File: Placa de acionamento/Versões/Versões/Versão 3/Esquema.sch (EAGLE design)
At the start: 23 parts, among them Q1 IRF540, Q2 IRF540, Q3 IRF540

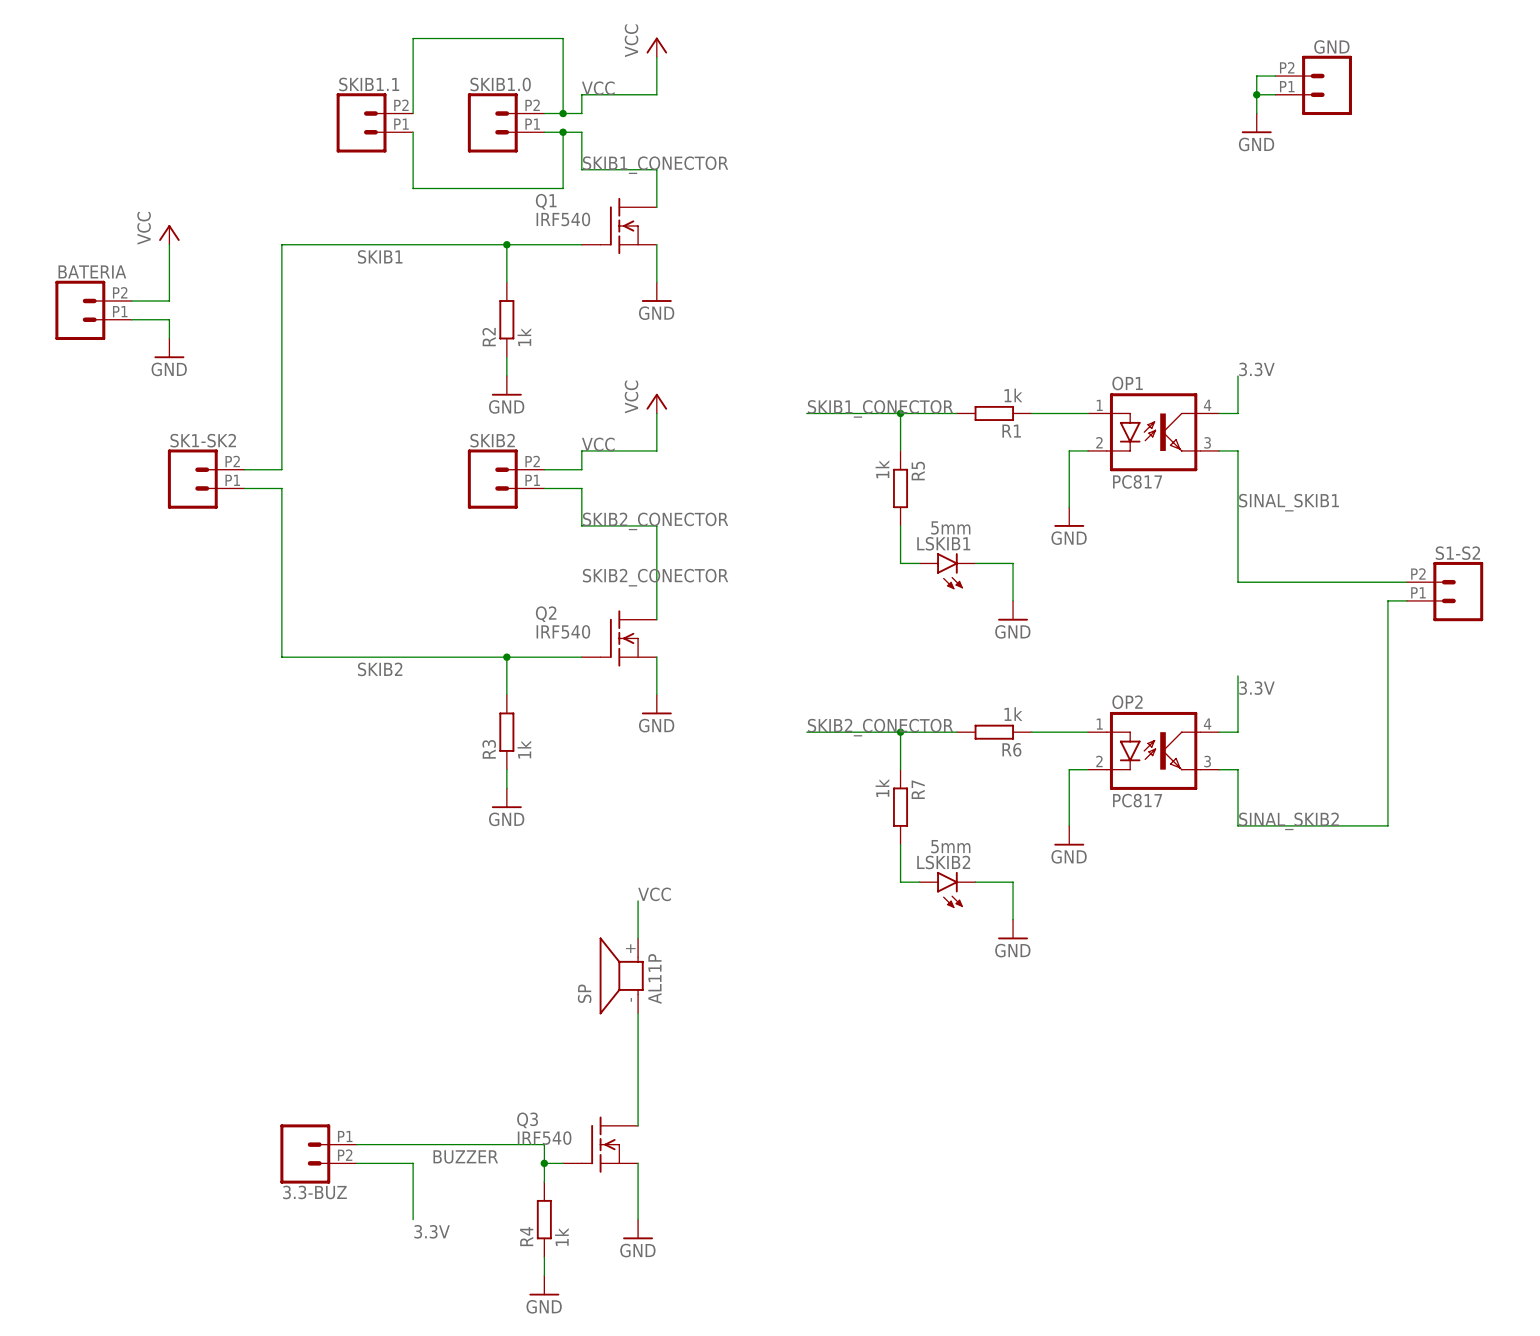
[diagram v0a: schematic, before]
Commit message: CHORE: trocando conectores JST
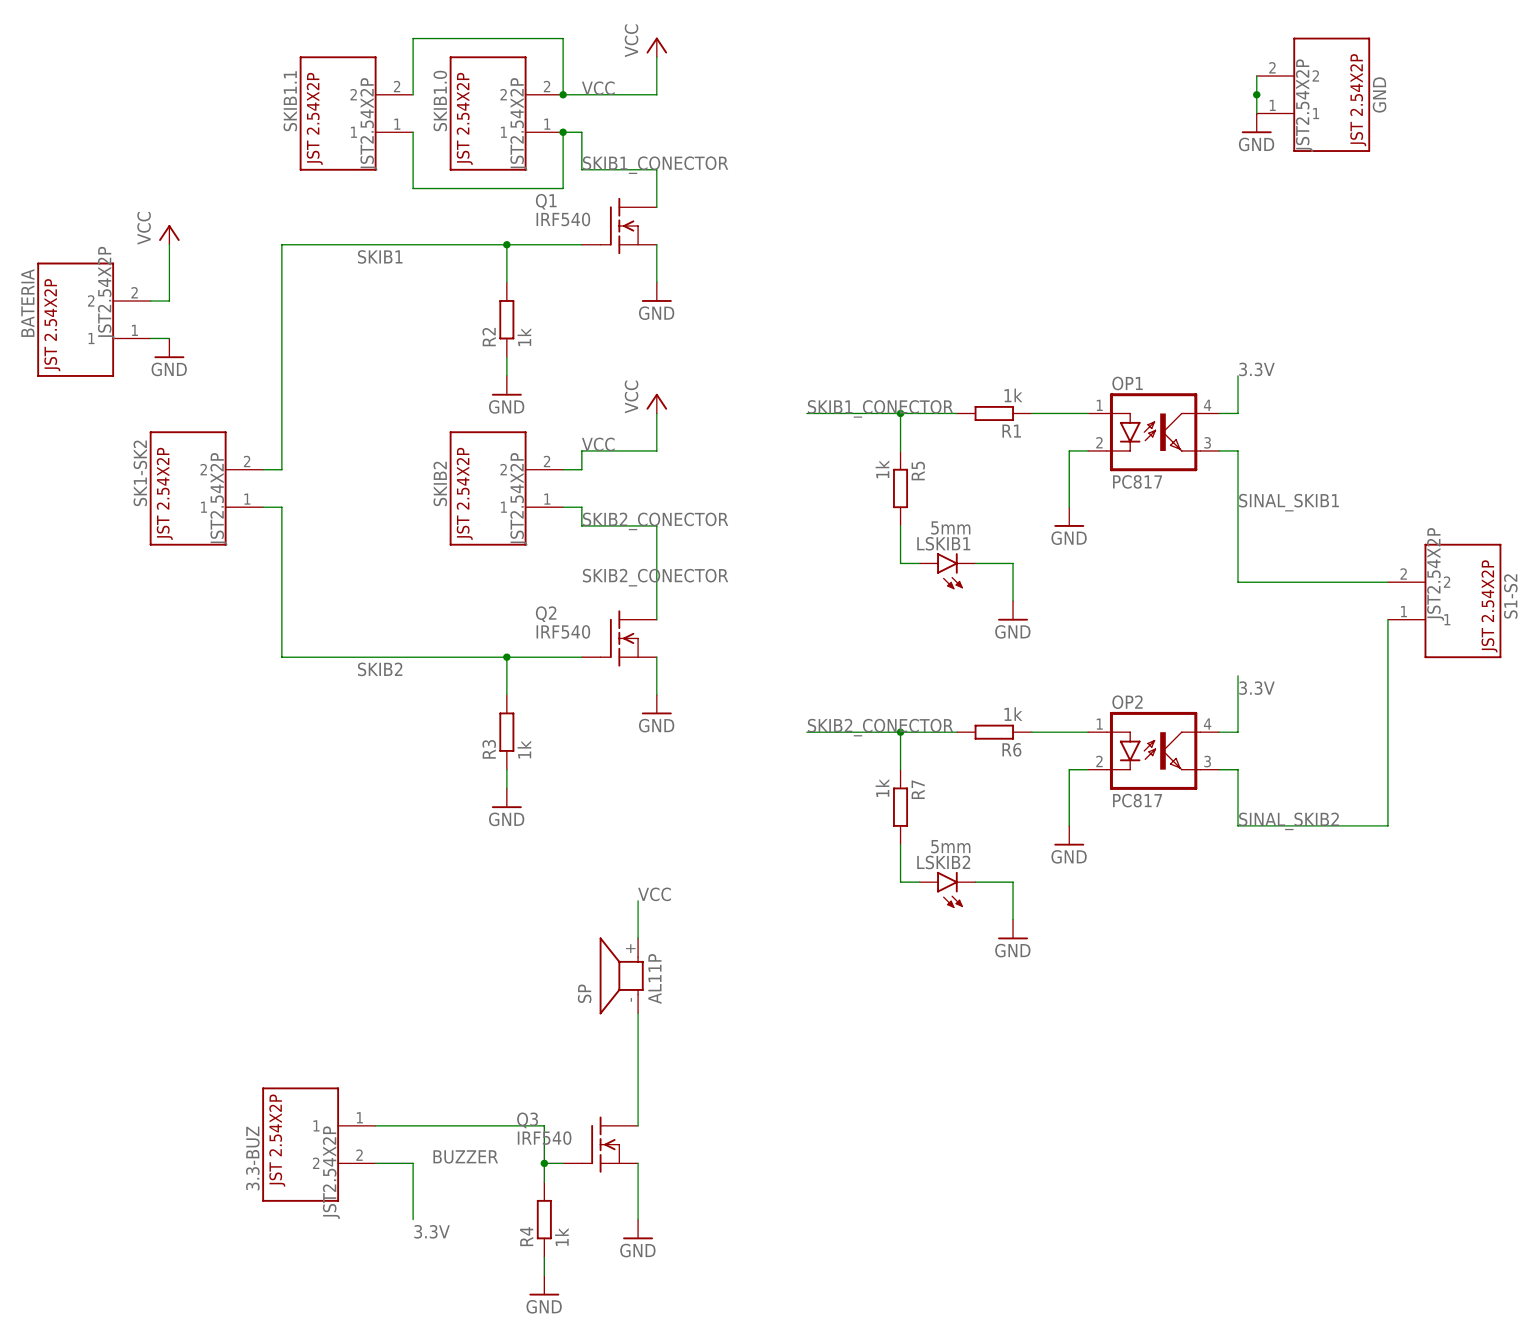
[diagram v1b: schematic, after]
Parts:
- 3.3-BUZ, BATERIA, GND, S1-S2, SK1-SK2, SKIB1.0, SKIB1.1, SKIB2: value (none) -> JST2.54X2P; device SparkFun-Connectors:CONN_022.54MM_SCREWTERM -> CRD:JST2.54X2P

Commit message: CHORE: adicionando pads ovais
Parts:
- LSKIB1, LSKIB2: device led:LED5MM -> led-modificada:LED5MM
- R1, R2, R3, R4, R5, R6, R7: device rcl:R-EU_0207/10 -> rcl-modificada:R-EU_0207/10
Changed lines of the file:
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@@
 <part name="Q3" library="transistor-fet" library_urn="urn:adsk.eagle:library:396" deviceset="IRF540" device="" package3d_urn="urn:adsk.eagle:package:28520/1" override_package3d_urn="urn:adsk.eagle:package:49474191/2" override_package_urn="urn:adsk.eagle:footprint:28453/1"/>
 <part name="GND2" library="supply1" library_urn="urn:adsk.eagle:library:371" deviceset="GND" device=""/>
-<part name="SP" library="buzzer" library_urn="urn:adsk.eagle:library:113" deviceset="AL11P" device="" package3d_urn="urn:adsk.eagle:package:5308/1" override_package3d_urn="urn:adsk.eagle:package:49474189/2" override_package_urn="urn:adsk.eagle:footprint:5250/1"/>
-<part name="R2" library="rcl" library_urn="urn:adsk.eagle:library:334" deviceset="R-EU_" device="0207/10" package3d_urn="urn:adsk.eagle:package:23491/2" value="1k"/>
-<part name="R3" library="rcl" library_urn="urn:adsk.eagle:library:334" deviceset="R-EU_" device="0207/10" package3d_urn="urn:adsk.eagle:package:23491/2" value="1k"/>
-<part name="R4" library="rcl" library_urn="urn:adsk.eagle:library:334" deviceset="R-EU_" device="0207/10" package3d_urn="urn:adsk.eagle:package:23491/2" value="1k"/>
+<part name="SP" library="buzzer" deviceset="AL11P" device="" package3d_urn="urn:adsk.eagle:package:5308/1" override_package3d_urn="urn:adsk.eagle:package:49474189/2" override_package_urn="urn:adsk.eagle:footprint:5250/1" override_locally_modified="yes"/>
+<part name="R2" library="rcl-modificada" deviceset="R-EU_" device="0207/10" package3d_urn="urn:adsk.eagle:package:23491/2" value="1k"/>
+<part name="R3" library="rcl-modificada" deviceset="R-EU_" device="0207/10" package3d_urn="urn:adsk.eagle:package:23491/2" value="1k"/>
+<part name="R4" library="rcl-modificada" deviceset="R-EU_" device="0207/10" package3d_urn="urn:adsk.eagle:package:23491/2" value="1k"/>
 <part name="GND1" library="supply1" library_urn="urn:adsk.eagle:library:371" deviceset="GND" device=""/>
 <part name="GND3" library="supply1" library_urn="urn:adsk.eagle:library:371" deviceset="GND" device=""/>
 <part name="GND4" library="supply1" library_urn="urn:adsk.eagle:library:371" deviceset="GND" device=""/>
 <part name="OP1" library="optocoupler" library_urn="urn:adsk.eagle:library:320" deviceset="PC817" device="" package3d_urn="urn:adsk.eagle:package:21938/1" override_package3d_urn="urn:adsk.eagle:package:49474184/2" override_package_urn="urn:adsk.eagle:footprint:21858/1"/>
-<part name="R1" library="rcl" library_urn="urn:adsk.eagle:library:334" deviceset="R-EU_" device="0207/10" package3d_urn="urn:adsk.eagle:package:23491/2" value="1k"/>
-<part name="R5" library="rcl" library_urn="urn:adsk.eagle:library:334" deviceset="R-EU_" device="0207/10" package3d_urn="urn:adsk.eagle:package:23491/2" value="1k"/>
-<part name="LSKIB1" library="led" library_urn="urn:adsk.eagle:library:259" deviceset="LED" device="5MM" package3d_urn="urn:adsk.eagle:package:15799/2" value="5mm"/>
+<part name="R1" library="rcl-modificada" deviceset="R-EU_" device="0207/10" package3d_urn="urn:adsk.eagle:package:23491/2" value="1k"/>
+<part name="R5" library="rcl-modificada" deviceset="R-EU_" device="0207/10" package3d_urn="urn:adsk.eagle:package:23491/2" value="1k"/>
+<part name="LSKIB1" library="led-modificada" deviceset="LED" device="5MM" package3d_urn="urn:adsk.eagle:package:15799/2" value="5mm"/>
 <part name="GND5" library="supply1" library_urn="urn:adsk.eagle:library:371" deviceset="GND" device=""/>
 <part name="GND7" library="supply1" library_urn="urn:adsk.eagle:library:371" deviceset="GND" device=""/>
 <part name="OP2" library="optocoupler" library_urn="urn:adsk.eagle:library:320" deviceset="PC817" device="" package3d_urn="urn:adsk.eagle:package:21938/1" override_package3d_urn="urn:adsk.eagle:package:49474187/2" override_package_urn="urn:adsk.eagle:footprint:21858/1"/>
-<part name="R6" library="rcl" library_urn="urn:adsk.eagle:library:334" deviceset="R-EU_" device="0207/10" package3d_urn="urn:adsk.eagle:package:23491/2" value="1k"/>
-<part name="R7" library="rcl" library_urn="urn:adsk.eagle:library:334" deviceset="R-EU_" device="0207/10" package3d_urn="urn:adsk.eagle:package:23491/2" value="1k"/>
-<part name="LSKIB2" library="led" library_urn="urn:adsk.eagle:library:259" deviceset="LED" device="5MM" package3d_urn="urn:adsk.eagle:package:15799/2" value="5mm"/>
+<part name="R6" library="rcl-modificada" deviceset="R-EU_" device="0207/10" package3d_urn="urn:adsk.eagle:package:23491/2" value="1k"/>
+<part name="R7" library="rcl-modificada" deviceset="R-EU_" device="0207/10" package3d_urn="urn:adsk.eagle:package:23491/2" value="1k"/>
+<part name="LSKIB2" library="led-modificada" deviceset="LED" device="5MM" package3d_urn="urn:adsk.eagle:package:15799/2" value="5mm"/>
 <part name="GND9" library="supply1" library_urn="urn:adsk.eagle:library:371" deviceset="GND" device=""/>
 <part name="GND11" library="supply1" library_urn="urn:adsk.eagle:library:371" deviceset="GND" device=""/>

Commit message: placa de acionamento
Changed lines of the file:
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@@
 <drawing>
 <settings>
-<setting alwaysvectorfont="no"/>
+<setting alwaysvectorfont="yes"/>
 <setting verticaltext="up"/>
 </settings>
@@
 <attribute name="NAME" x="165.608" y="83.82" size="1.778" layer="95" font="vector" rot="MR90"/>
 </instance>
-<instance part="GND12" gate="1" x="149.86" y="81.28" smashed="yes">
-<attribute name="VALUE" x="147.32" y="78.74" size="1.778" layer="96"/>
+<instance part="GND12" gate="1" x="149.86" y="78.74" smashed="yes">
+<attribute name="VALUE" x="147.32" y="76.2" size="1.778" layer="96"/>
 </instance>
 <instance part="BATERIA" gate="G$1" x="-10.16" y="55.88" smashed="yes" rot="R90">
@@
 </segment>
 <segment>
+<pinref part="GND" gate="G$1" pin="2"/>
+<pinref part="GND" gate="G$1" pin="1"/>
+<wire x1="149.86" y1="88.9" x2="149.86" y2="83.82" width="0.1524" layer="91"/>
 <pinref part="GND12" gate="1" pin="GND"/>
-<pinref part="GND" gate="G$1" pin="2"/>
-<wire x1="149.86" y1="86.36" x2="149.86" y2="88.9" width="0.1524" layer="91"/>
-<pinref part="GND" gate="G$1" pin="1"/>
-<wire x1="149.86" y1="83.82" x2="149.86" y2="86.36" width="0.1524" layer="91"/>
-<junction x="149.86" y="86.36"/>
+<wire x1="149.86" y1="83.82" x2="149.86" y2="81.28" width="0.1524" layer="91"/>
+<junction x="149.86" y="83.82"/>
 </segment>
 </net>
@@
 </sheet>
 </sheets>
-<errors>
-</errors>
 </schematic>
 </drawing>
